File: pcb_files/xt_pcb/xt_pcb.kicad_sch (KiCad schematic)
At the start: 31 parts, among them J1 Conn_01x04_Socket, J2 Conn_01x05, U1 XC6206PxxxMR, U2 RP2040, U3 W25Q128JVS, Y1 Crystal_GND24

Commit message: routing algorithm used
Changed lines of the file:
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@@
 (kicad_sch
-	(version 20231120)
+	(version 20250114)
 	(generator "eeschema")
-	(generator_version "8.0")
+	(generator_version "9.0")
 	(paper "A4")
 	(junction
@@
 		(at 251.46 21.59)
 		(size 12.7 3.81)
+		(exclude_from_sim no)
+		(in_bom yes)
+		(on_board yes)
+		(dnp no)
 		(fields_autoplaced yes)
 		(stroke
@@
 		)
 	)
+	(embedded_fonts no)
 )

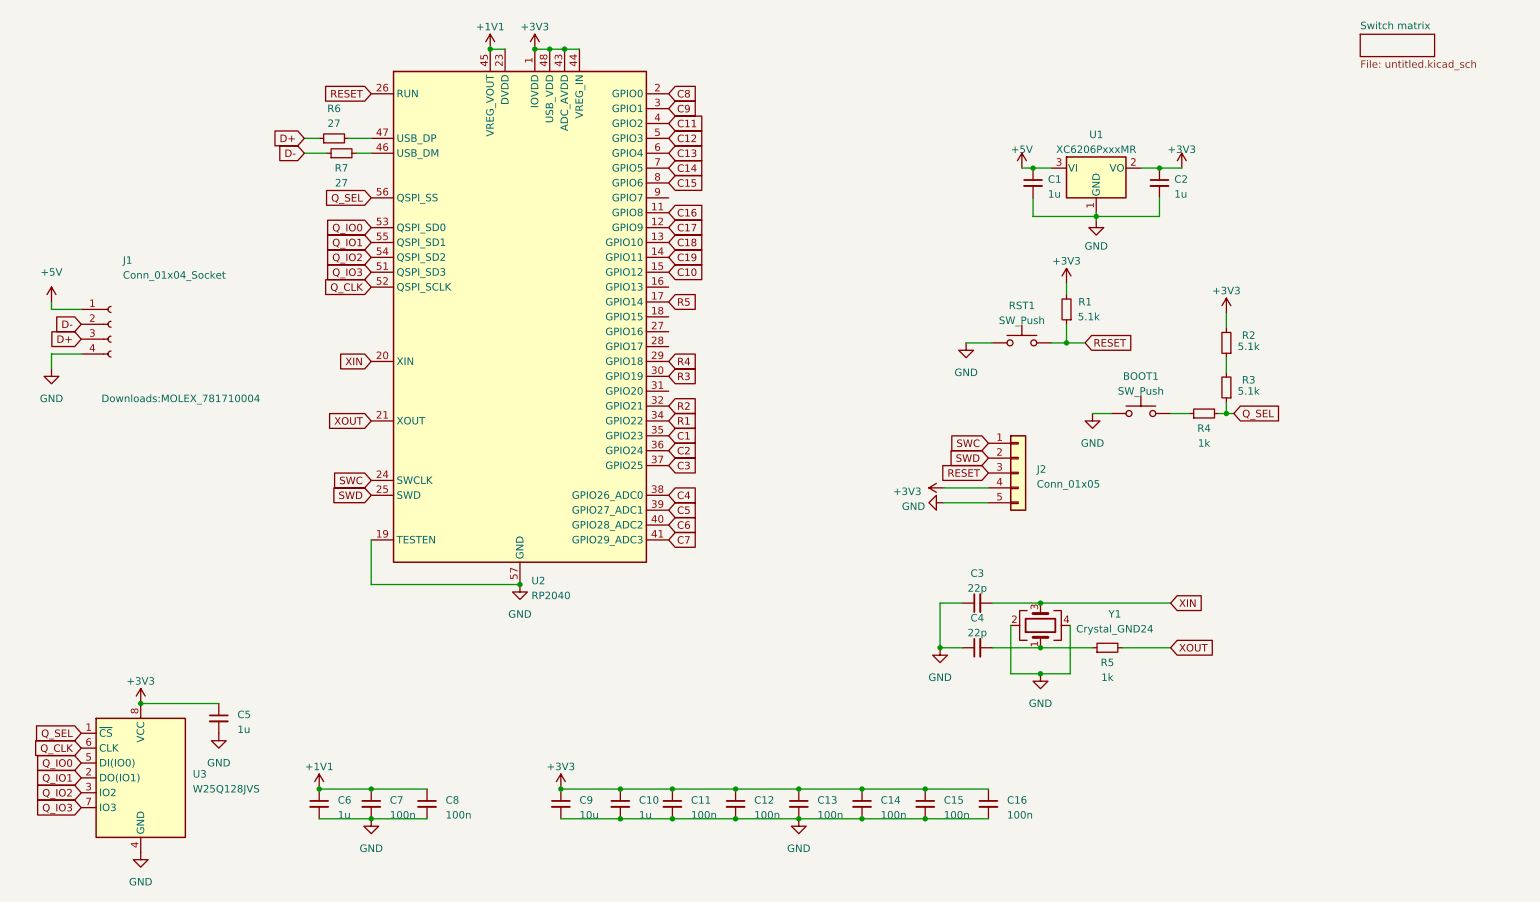
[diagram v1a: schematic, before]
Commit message: routing halluc. removed + usb c added
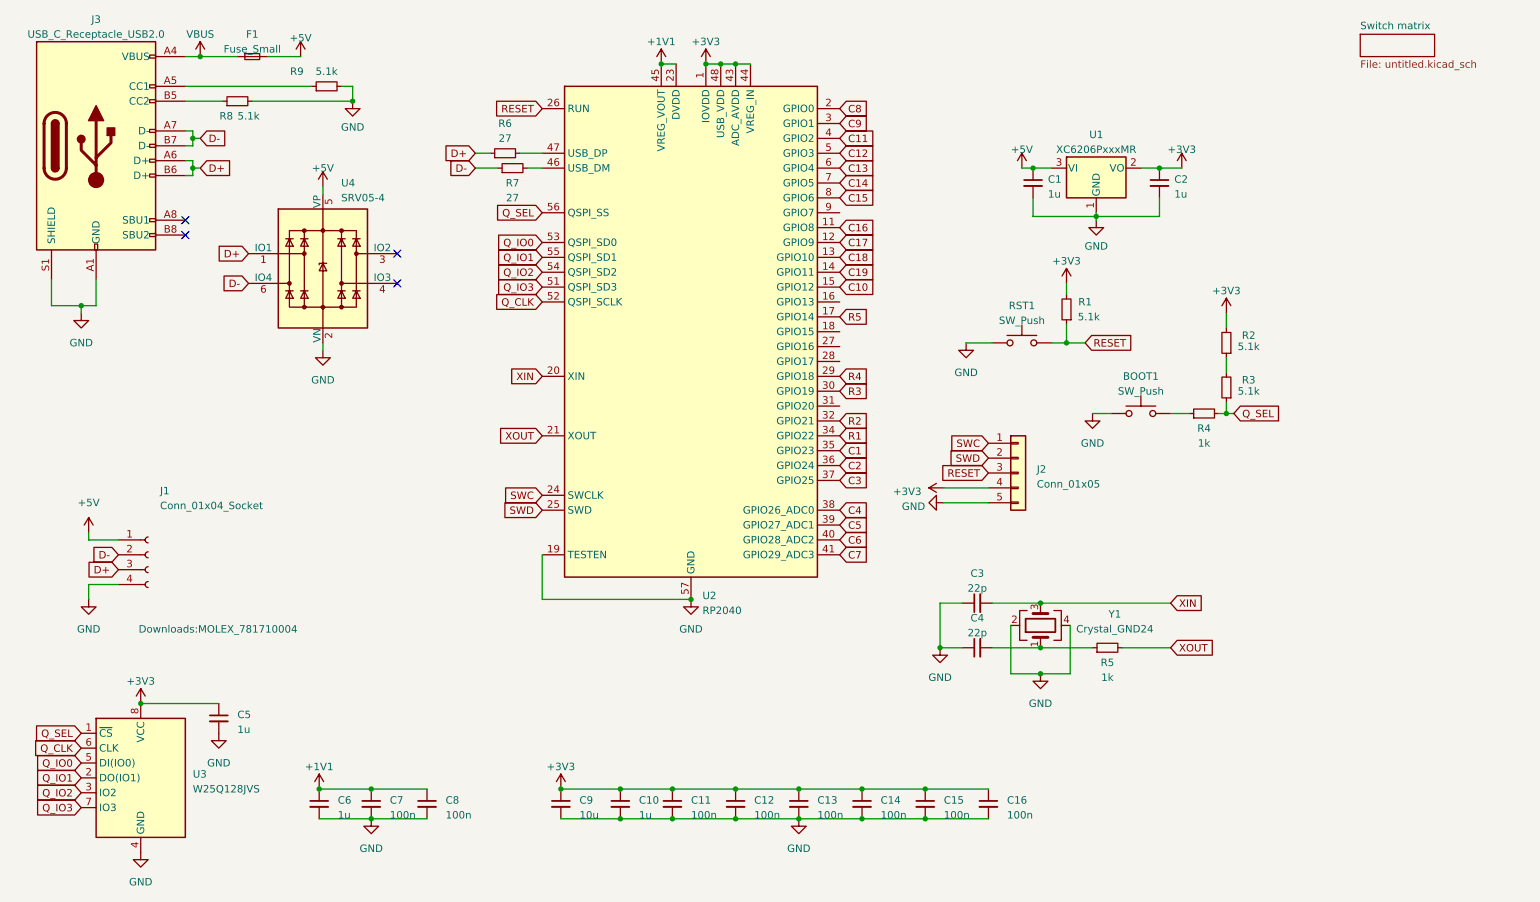
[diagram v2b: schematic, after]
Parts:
- added F1: Fuse_Small, Fuse:Fuse_1206_3216Metric, symbol Device:Fuse_Small
- added J3: USB_C_Receptacle_USB2.0, Connector_USB:USB_C_Receptacle_HRO_TYPE-C-31-M-12, symbol Connector:USB_C_Receptacle_USB2.0
- added R8, R9: 5.1k, Resistor_SMD:R_0402_1005Metric, symbol Device:R_Small
- added U4: SRV05-4, Package_TO_SOT_SMD:SOT-23-6_Handsoldering, symbol PCM_marbastlib-various:SRV05-4
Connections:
- net +5V: now also F1.2, U4.5 (VP)
- net D+: now also J3.A6 (D+), J3.B6 (D+), U4.1 (IO1)
- net D-: now also J3.A7 (D-), J3.B7 (D-), U4.6 (IO4)
- net GND: now also J3.A1 (GND), J3.A12 (GND), J3.B1 (GND), J3.B12 (GND), J3.S1 (SHIELD), R8.2, R9.2, U4.2 (VN)
- new net: J3.B5 (CC2), R8.1
- new net: J3.A5 (CC1), R9.1
- new net VBUS: F1.1, J3.A4 (VBUS), J3.A9 (VBUS), J3.B4 (VBUS), J3.B9 (VBUS)
- no-connect marks 0 -> 4
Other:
- moved on the sheet: J1, R6, R7, U2

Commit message: tweaks
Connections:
- net C8: now also U2.3 (GPIO1); no longer U2.2 (GPIO0)
- net C9: now also U2.2 (GPIO0); no longer U2.3 (GPIO1)

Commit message: vias removed
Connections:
- net C11: now also U2.5 (GPIO3); no longer U2.4 (GPIO2)
- net C12: now also U2.4 (GPIO2); no longer U2.5 (GPIO3)
- net C13: now also U2.11 (GPIO8); no longer U2.6 (GPIO4)
- net C14: now also U2.8 (GPIO6); no longer U2.7 (GPIO5)
- net C15: now also U2.7 (GPIO5); no longer U2.8 (GPIO6)
- net C16: now also U2.6 (GPIO4); no longer U2.11 (GPIO8)
- net C17: now also U2.14 (GPIO11); no longer U2.12 (GPIO9)
- net C19: now also U2.12 (GPIO9); no longer U2.14 (GPIO11)
- net C2: now also U2.34 (GPIO22); no longer U2.36 (GPIO24)
- net C3: now also U2.36 (GPIO24); no longer U2.37 (GPIO25)
- net C4: now also U2.32 (GPIO21); no longer U2.38 (GPIO26_ADC0)
- net C5: now also U2.30 (GPIO19); no longer U2.39 (GPIO27_ADC1)
- net C6: now also U2.39 (GPIO27_ADC1); no longer U2.40 (GPIO28_ADC2)
- net C7: now also U2.40 (GPIO28_ADC2); no longer U2.41 (GPIO29_ADC3)
- net R1: now also U2.37 (GPIO25); no longer U2.34 (GPIO22)
- net R2: now also U2.38 (GPIO26_ADC0); no longer U2.32 (GPIO21)
- net R3: now also U2.41 (GPIO29_ADC3); no longer U2.30 (GPIO19)

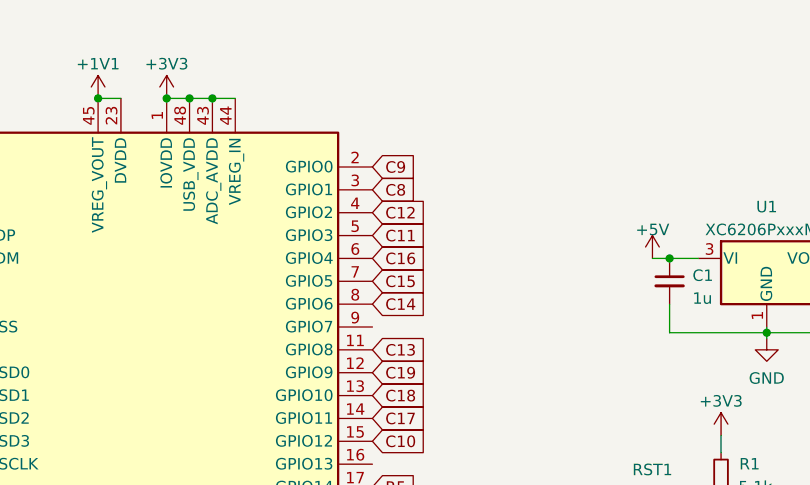
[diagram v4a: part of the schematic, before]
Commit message: cleaned up vias
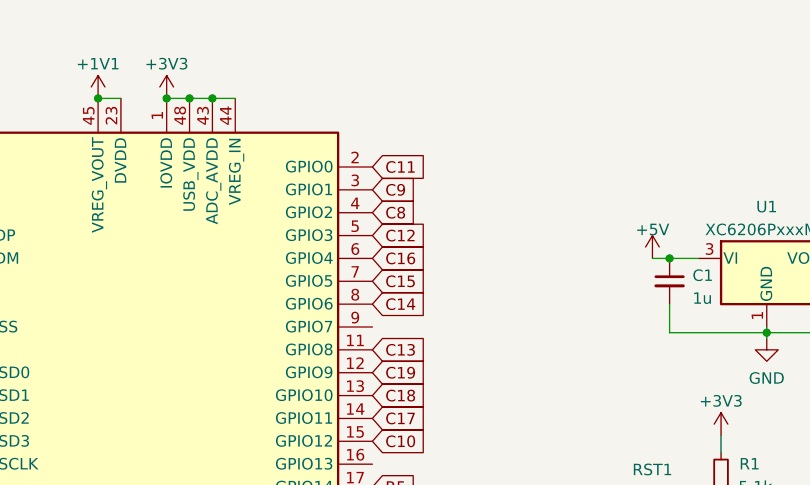
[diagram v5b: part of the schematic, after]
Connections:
- net C11: now also U2.2 (GPIO0); no longer U2.5 (GPIO3)
- net C12: now also U2.5 (GPIO3); no longer U2.4 (GPIO2)
- net C8: now also U2.4 (GPIO2); no longer U2.3 (GPIO1)
- net C9: now also U2.3 (GPIO1); no longer U2.2 (GPIO0)

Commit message: small sch tweaks
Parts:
- J1: footprint Downloads:MOLEX_781710004 -> Connector_Molex:Molex_Pico-EZmate_78171-0004_1x04-1MP_P1.20mm_Vertical
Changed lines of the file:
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@@
 			)
 		)
-		(property "Footprint" "Downloads:MOLEX_781710004"
+		(property "Footprint" "Connector_Molex:Molex_Pico-EZmate_78171-0004_1x04-1MP_P1.20mm_Vertical"
 			(at 56.388 123.19 0)
 			(effects
@@
 					(size 1.27 1.27)
 				)
+				(hide yes)
 			)
 		)

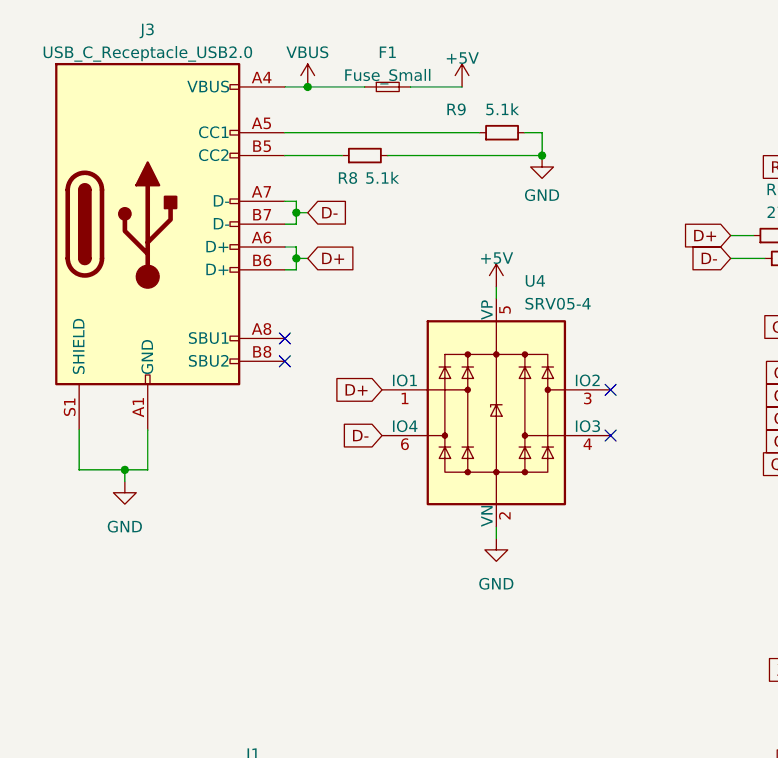
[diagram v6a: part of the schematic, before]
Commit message: fix: removed usb type c
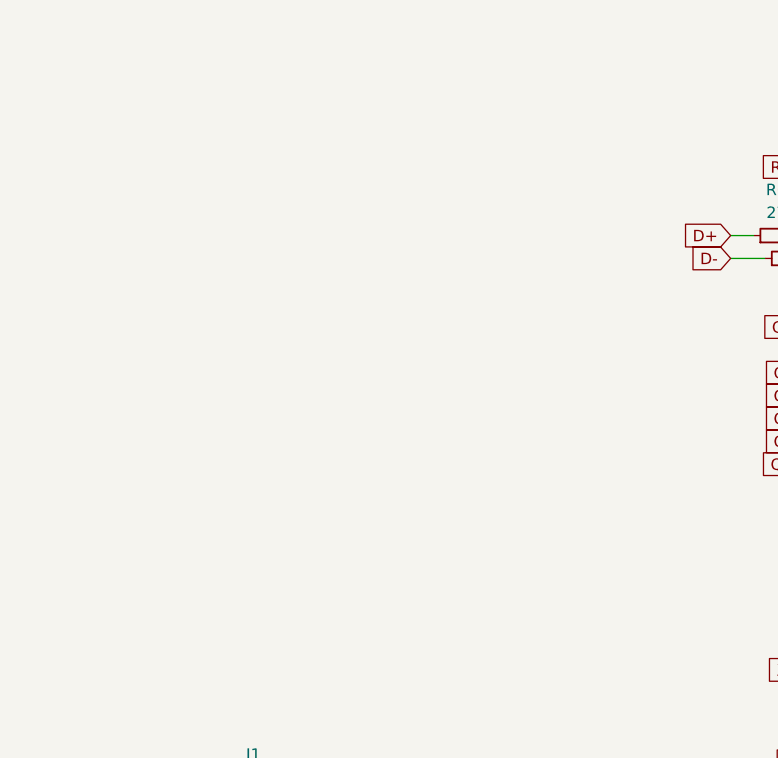
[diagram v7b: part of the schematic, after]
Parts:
- removed F1: Fuse_Small, Fuse:Fuse_1206_3216Metric, symbol Device:Fuse_Small
- removed J3: USB_C_Receptacle_USB2.0, Connector_USB:USB_C_Receptacle_HRO_TYPE-C-31-M-12, symbol Connector:USB_C_Receptacle_USB2.0
- removed R8, R9: 5.1k, Resistor_SMD:R_0402_1005Metric, symbol Device:R_Small
- removed U4: SRV05-4, Package_TO_SOT_SMD:SOT-23-6_Handsoldering, symbol PCM_marbastlib-various:SRV05-4
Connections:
- no-connect marks 4 -> 0

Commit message: feat: new stm32 based board in progress
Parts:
- removed BOOT1, RST1: SW_Push, Button_Switch_SMD:SW_SPST_TL3342, symbol Switch:SW_Push
- removed C10: 1u, Capacitor_SMD:C_0402_1005Metric, symbol Device:C_Small
- removed C11, C12, C13, C14, C15, C16: 100n, Capacitor_SMD:C_0402_1005Metric, symbol Device:C_Small
- removed J1: Conn_01x04_Socket, Connector_Molex:Molex_Pico-EZmate_78171-0004_1x04-1MP_P1.20mm_Vertical, symbol Connector:Conn_01x04_Socket
- removed J2: Conn_01x05, Connector_PinHeader_2.54mm:PinHeader_1x05_P2.54mm_Vertical, symbol Connector_Generic:Conn_01x05
- removed R2, R3: 5.1k, Resistor_SMD:R_0402_1005Metric, symbol Device:R_Small
- removed R4, R5: 1k, Resistor_SMD:R_0402_1005Metric, symbol Device:R_Small
- removed R6, R7: 27, Resistor_SMD:R_0402_1005Metric, symbol Device:R_Small
- removed U1: XC6206PxxxMR, Package_TO_SOT_SMD:SOT-23-3, symbol Regulator_Linear:XC6206PxxxMR
- removed U2: RP2040, Package_DFN_QFN:QFN-56-1EP_7x7mm_P0.4mm_EP3.2x3.2mm, symbol MCU_RaspberryPi:RP2040
- removed U3: W25Q128JVS, Package_SO:SOIC-8_5.23x5.23mm_P1.27mm, symbol Memory_Flash:W25Q128JVS
- removed Y1: Crystal_GND24, Crystal:Crystal_SMD_3225-4Pin_3.2x2.5mm, symbol Device:Crystal_GND24
- added J1: JST, Connector_Molex:Molex_Pico-EZmate_78171-0004_1x04-1MP_P1.20mm_Vertical, symbol Connector_Generic_MountingPin:Conn_01x04_MountingPin
- added SW1, SW2: RST, Button_Switch_SMD:SW_SPST_SKQG_WithoutStem, symbol Switch:SW_Push
- added U1: STM32F072C8Tx, Package_QFP:LQFP-48_7x7mm_P0.5mm, symbol MCU_ST_STM32F0:STM32F072C8Tx
- added U2: XC6206PxxxMR-Regulator_Linear, Package_TO_SOT_SMD:SOT-23, symbol kicad-keyboard-parts:XC6206PxxxMR-Regulator_Linear
- C1: value 1u -> 1uF; LCSC (none) -> C52923
- C2, C5, C6: value 1u -> 100nF; LCSC (none) -> C307331
- C3: value 22p -> 1uF; LCSC (none) -> C52923
- C4: value 22p -> 4.7uF; LCSC (none) -> C52923
- C7, C8: value 100n -> 100nF; LCSC (none) -> C307331
- C9: value 10u -> 100nF; footprint Capacitor_SMD:C_0603_1608Metric -> Capacitor_SMD:C_0402_1005Metric; LCSC (none) -> C307331
- R1: value 5.1k -> 10k
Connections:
- net +1V1 is gone; now on net +3V3: C6.1, C7.1, C8.1
- net RESET is gone; now on net GND: R1.1
- net XIN is gone; now on net +3V3: C3.2
- net +3V3: now also C4.1, SW1.1, U1.1 (VBAT), U1.24 (VDD), U1.36 (VDDIO2), U1.48 (VDD), U1.9 (VDDA), U2.2 (VO); no longer C2.1, R1.2
- net +5V: now also C1.2, J1.1 (Pin_1), U2.3 (VI); no longer C1.1
- net C1: now also U1.21 (PB10)
- net C10: now also U1.10 (PA0)
- net C11: now also U1.11 (PA1)
- net C12: now also U1.12 (PA2)
- net C13: now also U1.13 (PA3)
- net C14: now also U1.14 (PA4)
- net C15: now also U1.15 (PA5)
- net C16: now also U1.16 (PA6)
- net C17: now also U1.17 (PA7)
- net C18: now also U1.18 (PB0)
- net C19: now also U1.19 (PB1)
- net C2: now also U1.22 (PB11)
- net C3: now also U1.37 (PA14)
- net C4: now also U1.38 (PA15)
- net C5: now also U1.45 (PB8)
- net C6: now also U1.46 (PB9)
- net C7: now also U1.4 (PC15)
- net C8: now also U1.5 (PF0)
- net C9: now also U1.6 (PF1)
- net GND: now also C1.1, C2.1, C4.2, J1.4 (Pin_4), J1.MP (MountPin), SW2.1, U1.23 (VSS), U1.35 (VSS), U1.47 (VSS), U1.8 (VSSA), U2.1 (GND); no longer C1.2, C2.2, C4.1
- net R1: now also U1.28 (PB15)
- net R2: now also U1.27 (PB14)
- net R3: now also U1.26 (PB13)
- net R4: now also U1.25 (PB12)
- net R5: now also U1.20 (PB2)
- new net BOOT0: R1.2, SW1.2, U1.44 (BOOT0)
- new net D_N: J1.2 (Pin_2), U1.32 (PA11)
- new net D_P: J1.3 (Pin_3), U1.33 (PA12)
- new net NRST: C2.2, SW2.2, U1.7 (NRST)
- new net SWDCLK: U1.31 (PA10)
- new net SWDIO: U1.34 (PA13)
